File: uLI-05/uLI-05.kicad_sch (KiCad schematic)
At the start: 50 parts, among them J1 C, J2 USB_B, J3 RJ25, J4 RJ25, J5 PROG, Q1 IRF7306, U1 LM78M05_TO252, U2 PC817, U3 PC817, U4 PIC18F14K50-EP, U5 ADM2483xRW, Y1 12MHz

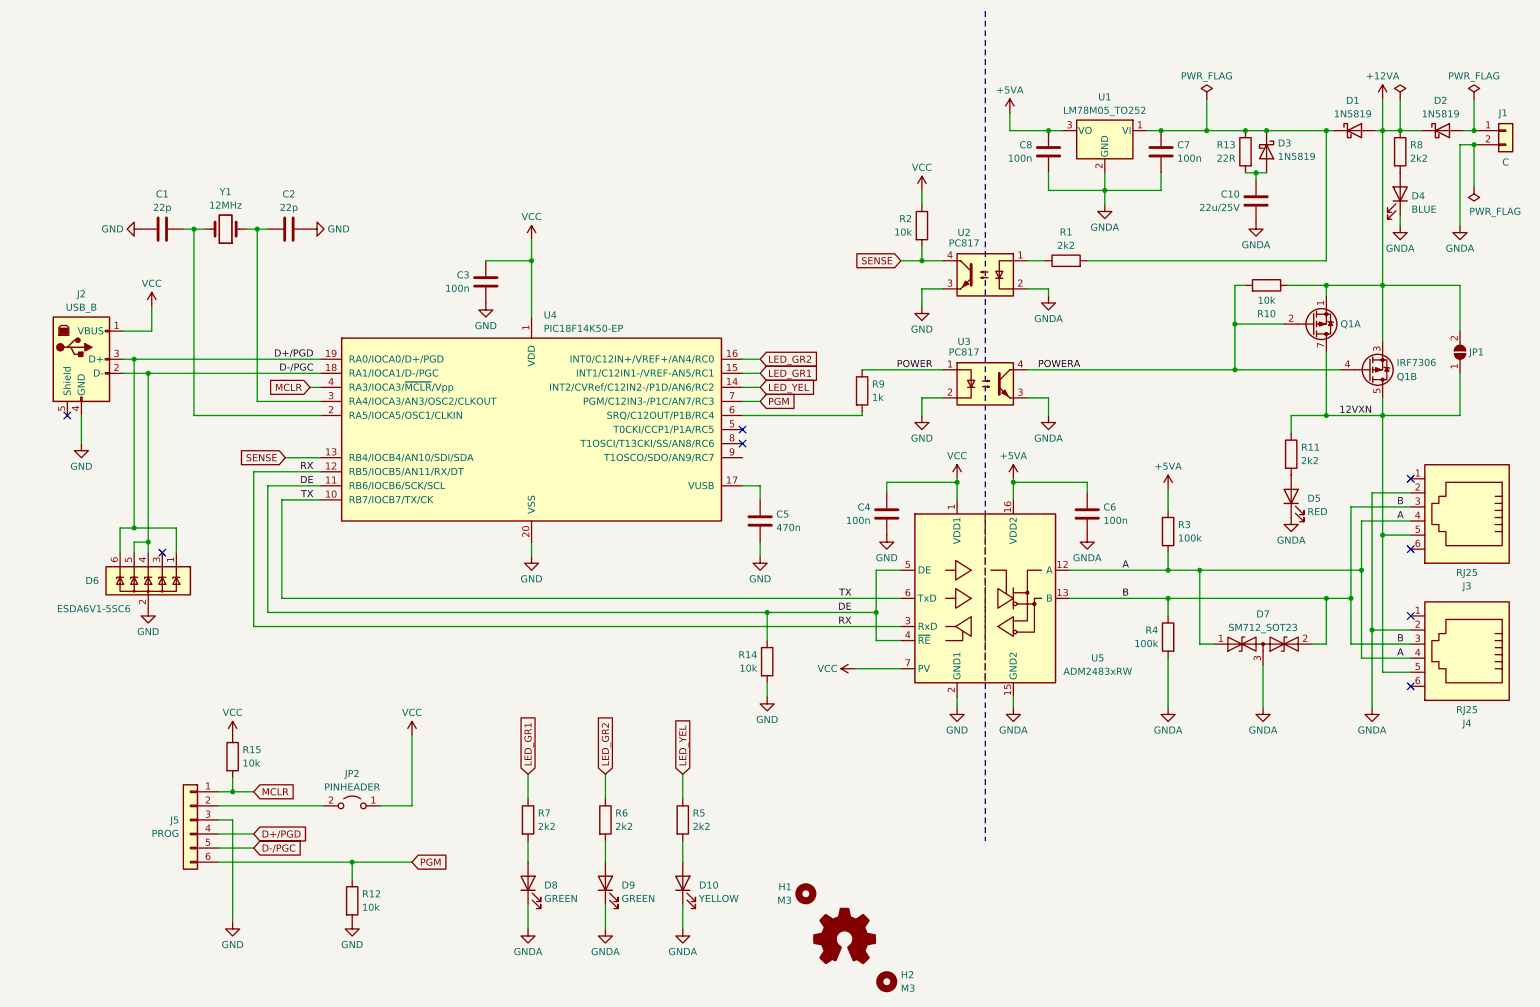
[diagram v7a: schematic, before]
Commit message: Use USBLC6 for USB protection.
Benefits:
* USBLC6 is specifically designed for USB
* It also protects VCC
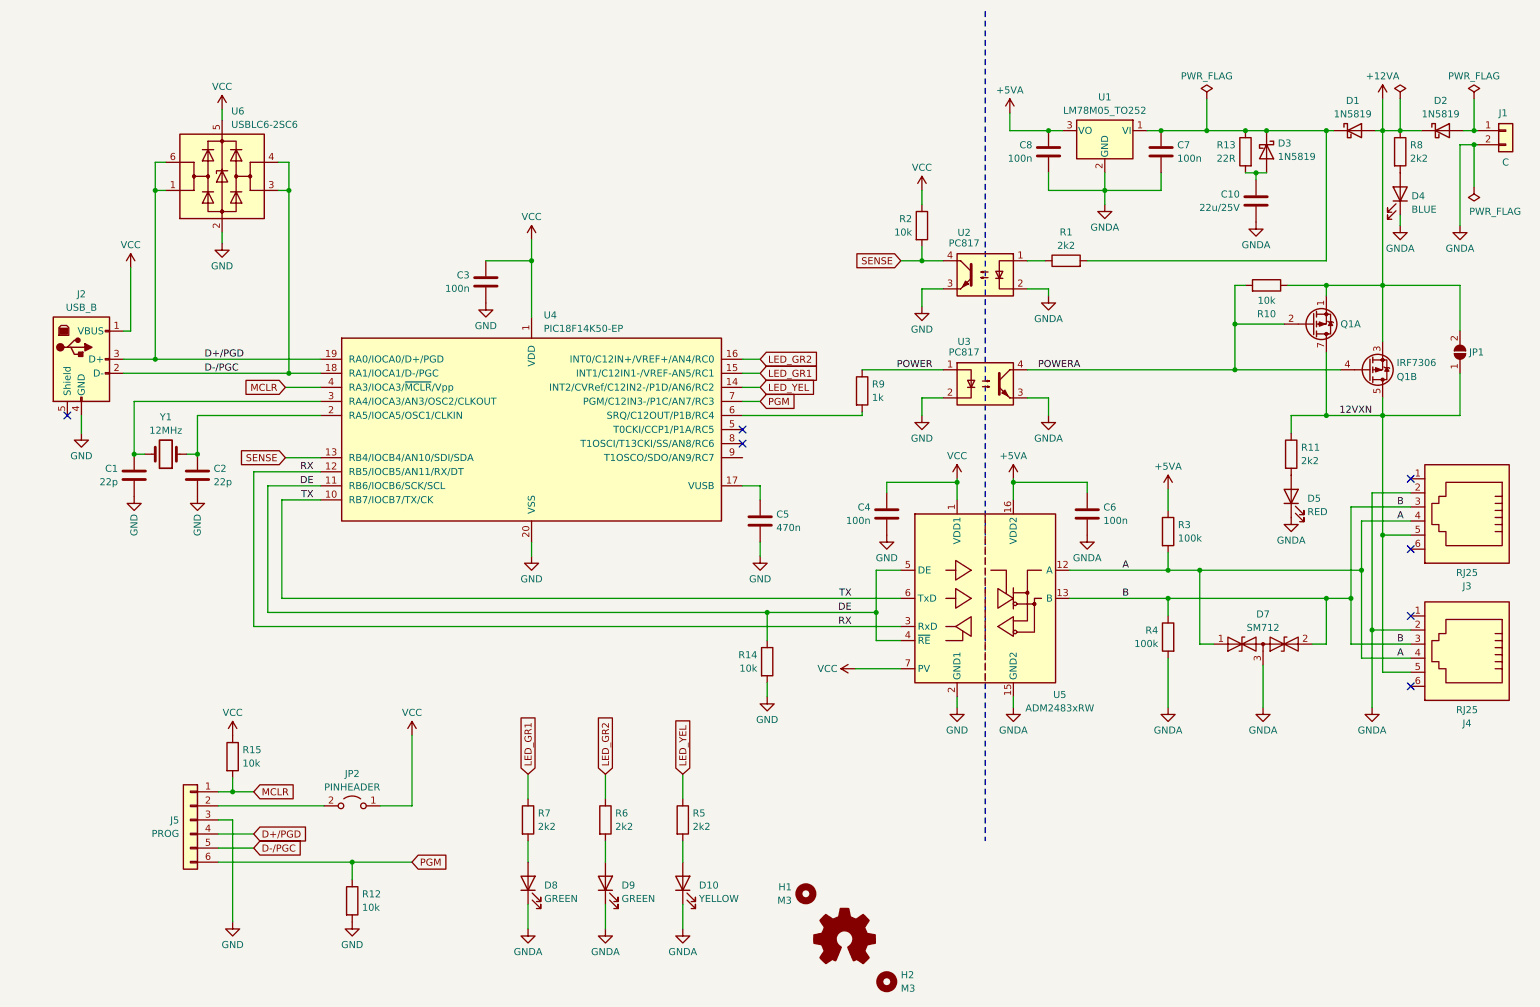
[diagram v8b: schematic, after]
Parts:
- removed D6: ESDA6V1-5SC6, Package_TO_SOT_SMD:SOT-23-6, symbol Power_Protection:ESDA6V1-5SC6
- added U6: USBLC6-2SC6, Package_TO_SOT_SMD:SOT-23-6, symbol Power_Protection:USBLC6-2SC6
- D7: value SM712_SOT23 -> SM712
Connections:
- net D+/PGD: now also U6.1 (I/O1), U6.6 (I/O1)
- net D-/PGC: now also U6.3 (I/O2), U6.4 (I/O2)
- net GND: now also C2.1, U6.2 (GND); no longer C2.2
- net VCC: now also U6.5 (VBUS)
- net at C1.2, Y1.2: now also U4.3 (RA4/IOCA3/AN3/OSC2/CLKOUT); no longer U4.2 (RA5/IOCA5/OSC1/CLKIN)
- new net: C2.2, U4.2 (RA5/IOCA5/OSC1/CLKIN), Y1.1
- no-connect marks 8 -> 7
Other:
- moved on the sheet: C1, C2, Y1
